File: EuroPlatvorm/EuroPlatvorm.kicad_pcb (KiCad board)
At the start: 2 copper layers, 32 parts, among them J1 Eurorack_Power_2x5, J2 USB_C_Receptacle_USB2.0, SW1 RST, SW2 BOOT, U1 TPS54202DDCR, U2 AMS1117-3.3, U3 USBLC6-2SC6, U4 ESP32-C6-WROOM-1-N4

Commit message: Fix tact switch footprint/symbol pin mismatch
- SW_TS-1187A footprint: renumber redundant legs to the switch's
  internal connection sets (left legs {1,3} -> pad 1, right legs
  {2,4} -> pad 2) so every pad carries a net
- PCB: applied same renumbering to placed SW1/SW2 instances and
  imported schematic net assignments via Update PCB from Schematic
- Resolves 'No net found for component SWx pad 3/4' warnings
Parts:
- added J3: Conn_01x14, Connector_PinHeader_2.54mm:PinHeader_1x14_P2.54mm_Vertical, F.Cu at (141.3, 69.8)
- added J4: Conn_01x14, Connector_PinHeader_2.54mm:PinHeader_1x14_P2.54mm_Vertical, F.Cu at (145.9, 69.8)
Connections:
- net Net-(U4-GPIO8) renamed /GPIO8
- net Net-(U4-GPIO9) renamed /GPIO9
- C10 pad 1: +3V3 -> GND
- C10 pad 2: GND -> +3V3
- C11 pad 1: +3V3 -> GND
- C11 pad 2: GND -> +3V3
- C6 pad 2: Net-(C6-Pad2) -> Net-(U1-FB)
- J1 pad 1: unconnected-(J1-Pin_1-Pad1) -> /-12V
- J1 pad 2: unconnected-(J1-Pin_2-Pad2) -> /-12V
- R1 pad 2: Net-(C6-Pad2) -> Net-(U1-FB)
- R2 pad 1: Net-(C6-Pad2) -> Net-(U1-FB)
- U1 pad 4: +3V3 -> Net-(U1-FB)
- U4 pad 11: unconnected-(U4-GPIO10-Pad11) -> /GPIO10
- U4 pad 12: unconnected-(U4-GPIO11-Pad12) -> /GPIO11
- U4 pad 16: unconnected-(U4-GPIO18-Pad16) -> /GPIO18
- U4 pad 17: unconnected-(U4-GPIO19-Pad17) -> /GPIO19
- U4 pad 18: unconnected-(U4-GPIO20-Pad18) -> /GPIO20
- U4 pad 19: unconnected-(U4-GPIO21-Pad19) -> /GPIO21
- U4 pad 20: unconnected-(U4-GPIO22-Pad20) -> /GPIO22
- U4 pad 21: unconnected-(U4-GPIO23-Pad21) -> /GPIO23
- U4 pad 23: unconnected-(U4-GPIO15-Pad23) -> /GPIO15
- U4 pad 24: unconnected-(U4-U0RXD/GPIO17-Pad24) -> /GPIO17
- U4 pad 25: unconnected-(U4-U0TXD/GPIO16-Pad25) -> /GPIO16
- U4 pad 26: unconnected-(U4-GPIO3/ADC1_CH3-Pad26) -> /GPIO3
- U4 pad 27: unconnected-(U4-GPIO2/ADC1_CH2-Pad27) -> /GPIO2
- U4 pad 4: unconnected-(U4-MTMS/GPIO4/ADC1_CH4-Pad4) -> /GPIO4
- U4 pad 5: unconnected-(U4-MTDI/GPIO5/ADC1_CH5-Pad5) -> /GPIO5
- U4 pad 6: unconnected-(U4-MTCK/GPIO6/ADC1_CH6-Pad6) -> /GPIO6
- U4 pad 7: unconnected-(U4-MTDO/GPIO7-Pad7) -> /GPIO7
- U4 pad 8: unconnected-(U4-GPIO0/ADC1_CH0/XTAL_32K_P-Pad8) -> /GPIO0
- U4 pad 9: unconnected-(U4-GPIO1/ADC1_CH1/XTAL_32K_N-Pad9) -> /GPIO1

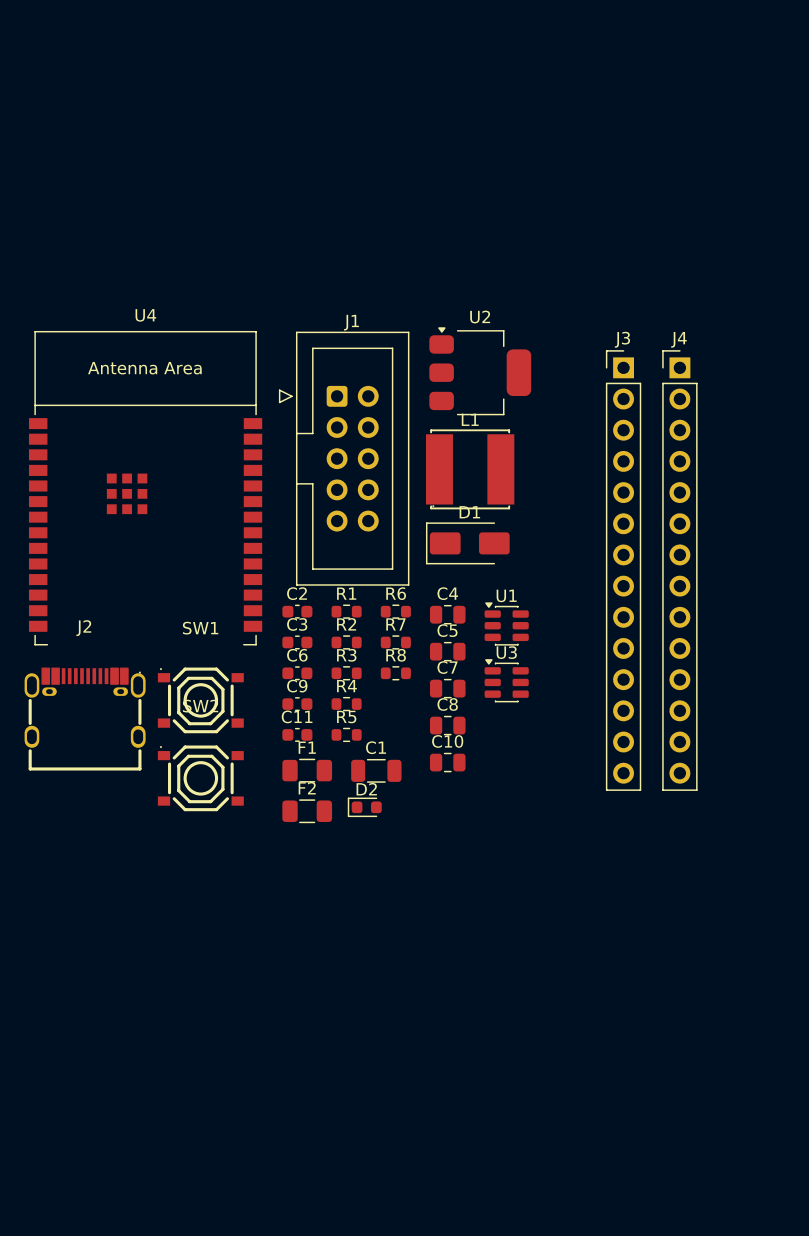
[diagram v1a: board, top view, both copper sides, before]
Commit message: Route EuroPlatvorm manually; fix GPIO labels and USB-C shell pad drills
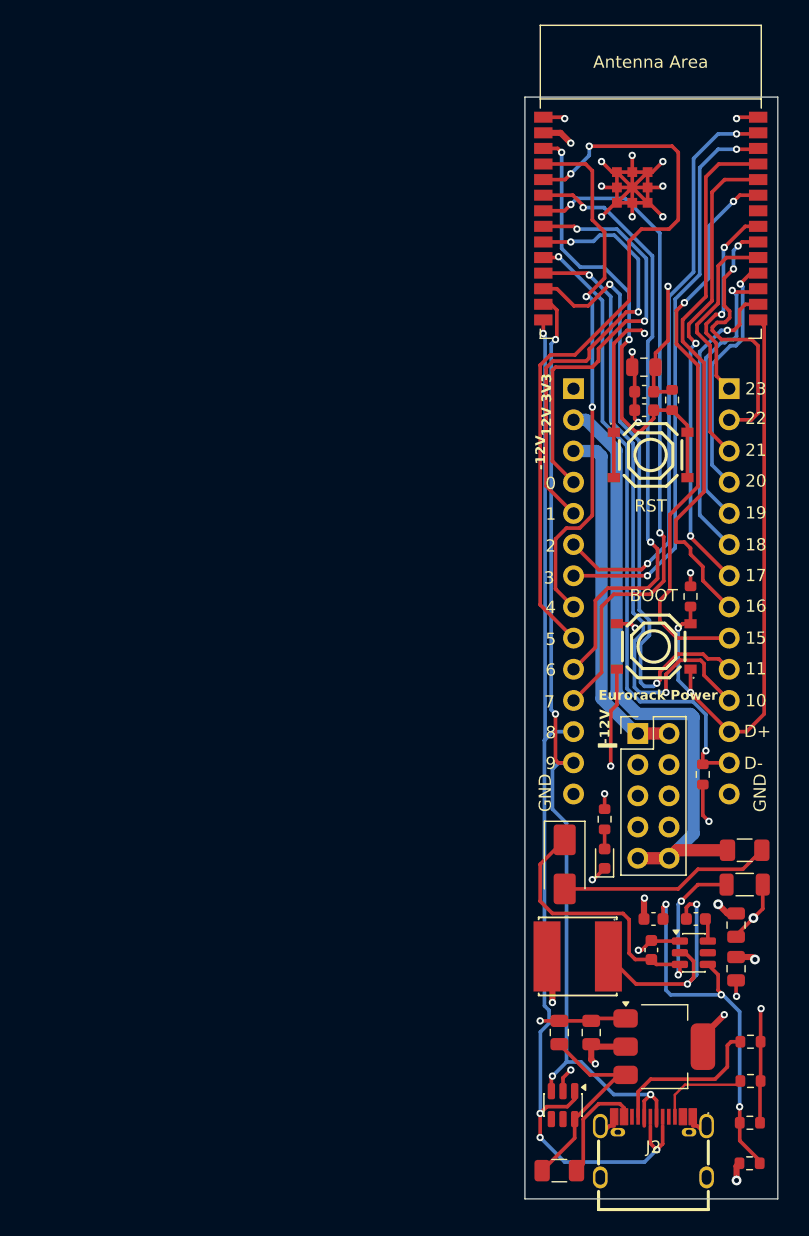
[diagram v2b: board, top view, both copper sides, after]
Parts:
- J1: footprint Connector_IDC:IDC-Header_2x05_P2.54mm_Vertical -> Connector_PinHeader_2.54mm:PinHeader_2x05_P2.54mm_Vertical
- J3, J4: moved to B.Cu
- moved J2 58.6 mm to (143.7, 133.3)
- moved U2 56.9 mm to (144.6, 125.1)
- moved R1 55.6 mm to (151.6, 134.6)
- moved R2 51.1 mm to (151.6, 131.3)
- moved U4 48.1 mm to (143.5, 57.6)
- moved R4 45.0 mm to (151.6, 127.9)
- moved R3 44.5 mm to (151.6, 124.7)
- moved SW1 41.7 mm to (143.5, 76.9)
- moved L1 40.6 mm to (137.6, 117.8), turned to 180 degrees
- moved C2 39.9 mm to (143.6, 117.2), turned to 90 degrees
- moved C11 39.7 mm to (143.0, 71.8)
- moved C3 39.5 mm to (147.2, 114.7)
- moved SW2 38.4 mm to (143.8, 92.5), turned to 180 degrees
- moved R5 38.0 mm to (145.2, 72.4), turned to -90 degrees
- moved C4 37.2 mm to (150.5, 118.8), turned to -90 degrees
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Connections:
- J3 pad 12: /GPIO10 -> /USB_DP
- J3 pad 13: /GPIO15 -> /USB_DM
- J4 pad 1: /GPIO18 -> /GPIO23
- J4 pad 10: /GPIO8 -> /GPIO11
- J4 pad 11: /GPIO11 -> /GPIO10
- J4 pad 12: /USB_DM -> /GPIO9
- J4 pad 13: /USB_DP -> /GPIO8
- J4 pad 2: /GPIO19 -> /GPIO22
- J4 pad 3: /GPIO20 -> /GPIO21
- J4 pad 4: /GPIO21 -> /GPIO20
- J4 pad 5: /GPIO22 -> /GPIO19
- J4 pad 6: /GPIO23 -> /GPIO18
- J4 pad 7: /GPIO16 -> /GPIO17
- J4 pad 8: /GPIO17 -> /GPIO16
- J4 pad 9: /GPIO9 -> /GPIO15
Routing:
- net GND: track 0.00 -> 99.9 mm, vias 0 -> 22
- net /USB_DP: track 0.00 -> 88.8 mm, vias 0 -> 4
- net /USB_DM: track 0.00 -> 82.5 mm, vias 0 -> 4
- net /GPIO5: track 0.00 -> 60.6 mm, vias 0 -> 2
- net /GPIO7: track 0.00 -> 54.1 mm, vias 0 -> 2
- net /GPIO8: track 0.00 -> 52.4 mm, vias 0 -> 2
- net +12V: track 0.00 -> 51.3 mm
- net /GPIO10: track 0.00 -> 51.3 mm, vias 0 -> 2
- net /GPIO9: track 0.00 -> 50.4 mm, vias 0 -> 2
- net /GPIO11: track 0.00 -> 50.1 mm, vias 0 -> 2
- net /GPIO6: track 0.00 -> 50.0 mm, vias 0 -> 2
- net /GPIO2: track 0.00 -> 47.8 mm, vias 0 -> 2
- net /GPIO15: track 0.00 -> 46.6 mm, vias 0 -> 2
- net /GPIO3: track 0.00 -> 46.4 mm, vias 0 -> 2
- net /GPIO16: track 0.00 -> 44.4 mm
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- added copper zone on In2.Cu, net +3V3
- added copper zone on In1.Cu, net GND
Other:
- board outline added: 20.6 x 89.8 mm
- copper layers 2 -> 4
- board text added: "-12V"
- board text added: "0"
- board text added: "1"
- board text added: "10"
- board text added: "11"
- board text added: "12V"
- board text added: "15"
- board text added: "16"
- board text added: "17"
- board text added: "18"
- board text added: "19"
- board text added: "2"
- board text added: "20"
- board text added: "21"
- board text added: "22"
- board text added: "23"
- board text added: "3"
- board text added: "3V3"
- board text added: "4"
- board text added: "5"
- board text added: "6"
- board text added: "7"
- board text added: "8"
- board text added: "9"
- board text added: "D+"
- board text added: "D-"
- board text added: "Eurorack Power"
- board text added: "GND"

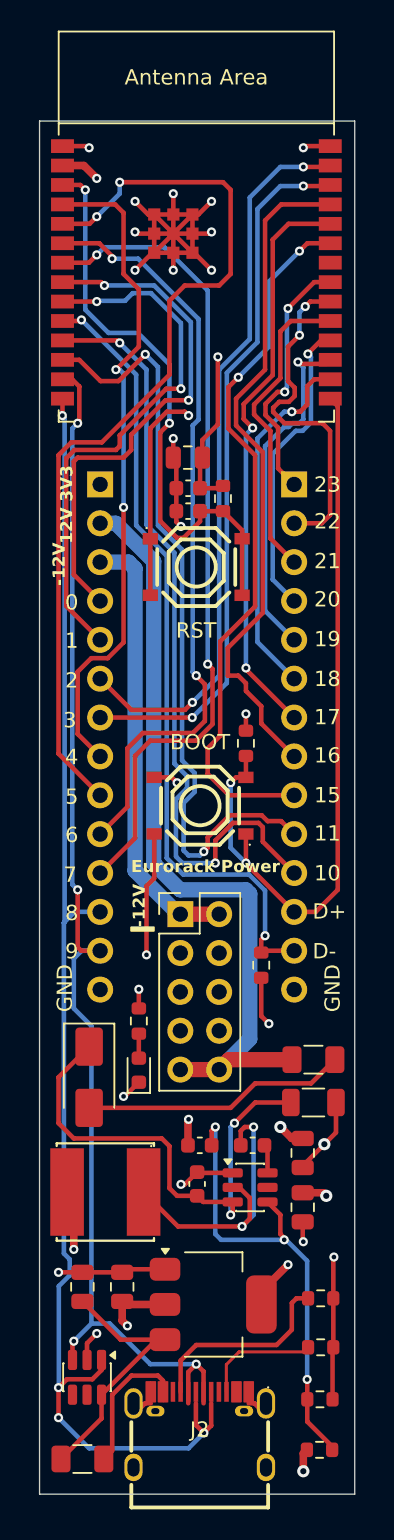
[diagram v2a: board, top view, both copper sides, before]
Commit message: Fix EMI review findings: C11 decoupling at 3V3 pin, buck SW/FB hot loop, USB routing, Vout to 3.3V
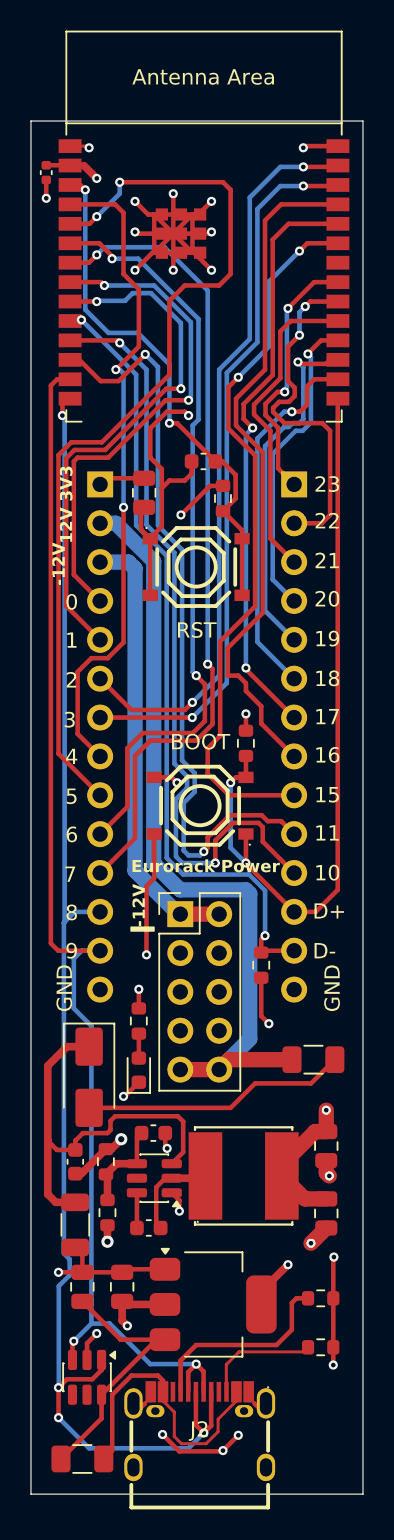
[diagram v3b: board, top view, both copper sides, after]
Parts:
- C11: footprint Capacitor_SMD:C_0603_1608Metric -> Capacitor_SMD:C_0402_1005Metric
- R2: value 21k -> 22k
- moved C11 22.6 mm to (133.7, 51.1), turned to 90 degrees
- moved R2 20.9 mm to (137.6, 115.8), turned to 90 degrees
- moved R1 20.8 mm to (137.7, 119.1), turned to 90 degrees
- moved C1 17.5 mm to (135.6, 119.9), turned to -90 degrees
- moved L1 9.10 mm to (146.6, 116.7), turned to 0 degrees
- moved C3 8.67 mm to (140.4, 120.1), turned to 180 degrees
- moved C2 8.09 mm to (135.6, 115.8), turned to -90 degrees
- moved U1 6.29 mm to (140.8, 116.8), turned to 180 degrees
- moved C10 3.66 mm to (140.1, 72.0), turned to 90 degrees
- moved C9 3.40 mm to (144.0, 70.0)
- moved C6 3.14 mm to (140.7, 113.9), turned to 180 degrees
- moved C5 1.60 mm to (152.0, 114.8)
- moved C4 1.59 mm to (152.0, 119.2)
- moved U4 0.50 mm to (144.0, 57.6)
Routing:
- net Net-(U1-FB): track 31.0 -> 6.16 mm, vias 3 -> 0
- net Net-(U1-SW): track 19.5 -> 6.30 mm, vias 2 -> 0
- net Net-(F2-Pad2): track 9.13 -> 18.8 mm
- net Net-(U4-EN/CHIP_PU): track 38.6 -> 33.6 mm
- net Net-(D1-K): track 32.2 -> 27.6 mm, vias 2 -> 0
- net +3V3: track 37.3 -> 34.2 mm, vias 12 -> 10
- net GND: track 99.9 -> 102.8 mm, vias 22 -> 26
- net /USB_DP: track 88.8 -> 90.3 mm
- net /GPIO8: track 52.4 -> 51.2 mm
- net /GPIO11: track 50.1 -> 49.0 mm
- net /GPIO9: track 50.4 -> 49.7 mm
- net /GPIO0: track 34.2 -> 33.6 mm
- net /USB_DM: track 82.5 -> 82.6 mm, vias 4 -> 2
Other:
- board size 20.6 x 89.8 mm -> 21.7 x 89.8 mm

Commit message: Harden USB-C footprint, add stitching and LDO thermal vias; relax edge clearance to 0.3mm
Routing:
- net GND: track 102.8 -> 95.7 mm, vias 26 -> 28
- net +3V3: vias 10 -> 14
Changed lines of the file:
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@@
 			)
 		)
-		(pad "" thru_hole oval
+		(pad "" np_thru_hole oval
 			(at -2.9 -1.21)
-			(size 1.2 0.8)
+			(size 0.55 0.5)
 			(drill oval 0.55 0.5)
 			(layers "*.Cu" "*.Mask")
-			(remove_unused_layers no)
 		)
-		(pad "" thru_hole oval
+		(pad "" np_thru_hole oval
 			(at 2.9 -1.21)
-			(size 1.2 0.8)
+			(size 0.55 0.5)
 			(drill oval 0.55 0.5)
 			(layers "*.Cu" "*.Mask")
-			(remove_unused_layers no)
 		)
 		(pad "1" thru_hole oval
@@
 				(gr_poly
 					(pts
-						(xy 0.299923 0.649935) (xy 0.299923 -0.650088) (xy -0.000076 -0.650088) (xy -0.000076 -0.649935)
-						(xy -0.30005 -0.649935) (xy -0.30005 0.650088) (xy -0.000051 0.650088) (xy -0.000051 0.649935)
-						(xy 0.299923 0.649935)
+						(xy 0.15 0.649935) (xy 0.15 -0.650088) (xy -0.000076 -0.650088) (xy -0.000076 -0.649935) (xy -0.30005 -0.649935)
+						(xy -0.30005 0.650088) (xy -0.000051 0.650088) (xy -0.000051 0.649935) (xy 0.15 0.649935)
 					)
 					(width 0.1)
@@
 				(gr_poly
 					(pts
-						(xy 0.300076 0.650037) (xy 0.300076 -0.649935) (xy 0.000051 -0.649935) (xy 0.000051 -0.64991)
-						(xy -0.299898 -0.64991) (xy -0.299898 0.650062) (xy 0.000127 0.650062) (xy 0.000127 0.650037)
-						(xy 0.300076 0.650037)
+						(xy 0.24 0.650037) (xy 0.24 -0.649935) (xy 0.000051 -0.649935) (xy 0.000051 -0.64991) (xy -0.2 -0.64991)
+						(xy -0.2 0.650062) (xy 0.000127 0.650062) (xy 0.000127 0.650037) (xy 0.24 0.650037)
 					)
 					(width 0.1)
@@
 				(gr_poly
 					(pts
-						(xy -0.300152 -0.650088) (xy -0.300152 0.649884) (xy -0.000152 0.649884) (xy -0.000127 0.649884)
-						(xy 0.299872 0.649884) (xy 0.299872 -0.650088) (xy -0.000127 -0.650088) (xy -0.000152 -0.650088)
-						(xy -0.300152 -0.650088)
+						(xy -0.15 -0.650088) (xy -0.15 0.649884) (xy -0.000152 0.649884) (xy -0.000127 0.649884) (xy 0.299872 0.649884)
+						(xy 0.299872 -0.650088) (xy -0.000127 -0.650088) (xy -0.000152 -0.650088) (xy -0.15 -0.650088)
 					)
 					(width 0.1)
@@
 				(gr_poly
 					(pts
-						(xy 0.299872 0.649884) (xy 0.299872 -0.650088) (xy -0.000127 -0.650088) (xy -0.000152 -0.650088)
-						(xy -0.300152 -0.650088) (xy -0.300152 0.649884) (xy -0.000152 0.649884) (xy -0.000127 0.649884)
-						(xy 0.299872 0.649884)
+						(xy 0.2 0.649884) (xy 0.2 -0.650088) (xy -0.000127 -0.650088) (xy -0.000152 -0.650088) (xy -0.24 -0.650088)
+						(xy -0.24 0.649884) (xy -0.000152 0.649884) (xy -0.000127 0.649884) (xy 0.2 0.649884)
 					)
 					(width 0.1)
@@
 	)
 	(segment
-		(start 146.25 133.65)
-		(end 145.25 134.65)
-		(width 0.3)
-		(layer "F.Cu")
-		(net "GND")
-	)
-	(segment
 		(start 141.9 90.65)
 		(end 142.25 91)
@@
 	)
 	(segment
+		(start 147.69 131.57)
+		(end 146.93 130.81)
+		(width 0.2)
+		(layer "F.Cu")
+		(net "GND")
+	)
+	(segment
 		(start 139.61 55.11)
 		(end 139.5 55)
@@
 	)
 	(segment
-		(start 142.005 55.11)
-		(end 140.755 53.86)
+		(start 135.6 116.55)
+		(end 135.6 117.2)
 		(width 0.3)
 		(layer "F.Cu")
@@
 	)
 	(segment
-		(start 141.3 133.6)
-		(end 142.4 134.7)
+		(start 142.005 55.11)
+		(end 140.755 53.86)
 		(width 0.3)
 		(layer "F.Cu")
@@
 	)
 	(segment
-		(start 136 116.55)
-		(end 137.6 114.95)
-		(width 0.5)
-		(layer "F.Cu")
-		(net "GND")
-	)
-	(segment
 		(start 143.255 53.86)
 		(end 143.64 53.86)
@@
 	)
 	(segment
+		(start 139.4 131.57)
+		(end 139.77 131.57)
+		(width 0.2)
+		(layer "F.Cu")
+		(net "GND")
+	)
+	(segment
 		(start 138.75 111.5)
 		(end 138.825 111.5)
@@
 	)
 	(segment
-		(start 142.4 134.7)
-		(end 145.2 134.7)
-		(width 0.3)
-		(layer "F.Cu")
-		(net "GND")
-	)
-	(segment
 		(start 138.66 123)
 		(end 136.06 123)
@@
 	)
 	(segment
+		(start 148.06 131.57)
+		(end 147.69 131.57)
+		(width 0.2)
+		(layer "F.Cu")
+		(net "GND")
+	)
+	(segment
 		(start 141.25 71.75)
 		(end 141.25 70.5)
@@
 	)
 	(segment
-		(start 140.16 131.56)
-		(end 139.4 132.32)
-		(width 0.3)
-		(layer "F.Cu")
-		(net "GND")
-	)
-	(segment
 		(start 152.26 49.39)
 		(end 150.61 49.39)
@@
 	)
 	(segment
-		(start 142.005 53.86)
-		(end 142.005 52.505)
-		(width 0.3)
+		(start 139.77 131.57)
+		(end 140.53 130.81)
+		(width 0.2)
 		(layer "F.Cu")
 		(net "GND")
 	)
 	(segment
-		(start 140.755 56.36)
-		(end 142.005 55.11)
+		(start 142.005 53.86)
+		(end 142.005 52.505)
 		(width 0.3)
 		(layer "F.Cu")
@@
 	)
 	(segment
-		(start 145.25 134.65)
-		(end 145.2 134.7)
+		(start 140.755 56.36)
+		(end 142.005 55.11)
 		(width 0.3)
 		(layer "F.Cu")
@@
 	)
 	(segment
-		(start 135.6 116.55)
-		(end 136 116.55)
-		(width 0.5)
-		(layer "F.Cu")
-		(net "GND")
-	)
-	(segment
 		(start 140.75 94.35)
 		(end 140.75 97.25)
@@
 	)
 	(segment
-		(start 147.3 131.56)
-		(end 148.06 132.32)
-		(width 0.3)
-		(layer "F.Cu")
-		(net "GND")
-	)
-	(segment
 		(start 140.25 97.75)
 		(end 140.25 102.25)
@@
 	)
 	(via
+		(at 133.3 132.5)
+		(size 0.6)
+		(drill 0.3)
+		(layers "F.Cu" "B.Cu")
+		(free yes)
+		(net "GND")
+	)
+	(via
 		(at 143 67)
 		(size 0.6)
@@
 	)
 	(via
-		(at 145.25 134.65)
+		(at 152.5 122)
 		(size 0.6)
 		(drill 0.3)
 		(layers "F.Cu" "B.Cu")
+		(free yes)
 		(net "GND")
 	)
 	(via
-		(at 152.5 122)
+		(at 144.5 53)
 		(size 0.6)
 		(drill 0.3)
@@
 	)
 	(via
-		(at 144.5 53)
+		(at 139.5 55)
 		(size 0.6)
 		(drill 0.3)
@@
 	)
 	(via
-		(at 139.5 55)
+		(at 133.35 67)
 		(size 0.6)
 		(drill 0.3)
@@
 	)
 	(via
-		(at 138.75 111.5)
+		(at 144 135)
 		(size 0.6)
 		(drill 0.3)
@@
 	)
 	(via
-		(at 150.5 49.5)
+		(at 138.75 111.5)
 		(size 0.6)
 		(drill 0.3)
@@
 	)
 	(via
-		(at 146.25 133.65)
+		(at 135.6 117.2)
 		(size 0.6)
 		(drill 0.3)
@@
 	)
 	(via
+		(at 150.5 49.5)
+		(size 0.6)
+		(drill 0.3)
+		(layers "F.Cu" "B.Cu")
+		(free yes)
+		(net "GND")
+	)
+	(via
 		(at 133.7 52.8)
 		(size 0.6)
@@
 	)
 	(via
-		(at 142.4 119)
+		(at 133.4 130.6)
 		(size 0.6)
 		(drill 0.3)
 		(layers "F.Cu" "B.Cu")
+		(free yes)
 		(net "GND")
 	)
 	(via
-		(at 136.5 49.5)
+		(at 142.4 119)
 		(size 0.6)
 		(drill 0.3)
 		(layers "F.Cu" "B.Cu")
-		(free yes)
 		(net "GND")
 	)
 	(via
-		(at 142.25 91)
+		(at 136.5 49.5)
 		(size 0.6)
 		(drill 0.3)
 		(layers "F.Cu" "B.Cu")
+		(free yes)
 		(net "GND")
 	)
 	(via
-		(at 141.3 133.6)
+		(at 142.25 91)
 		(size 0.6)
 		(drill 0.3)
@@
 	)
 	(via
+		(at 147.16 126.05)
+		(size 0.6)
+		(drill 0.3)
+		(layers "F.Cu" "B.Cu")
+		(net "+3V3")
+	)
+	(via
 		(at 137 51.5)
 		(size 0.6)
@@
 	)
 	(via
+		(at 148.36 124.15)
+		(size 0.6)
+		(drill 0.3)
+		(layers "F.Cu" "B.Cu")
+		(net "+3V3")
+	)
+	(via
 		(at 142.5 73.5)
 		(size 0.6)
@@
 	)
 	(via
+		(at 147.16 124.15)
+		(size 0.6)
+		(drill 0.3)
+		(layers "F.Cu" "B.Cu")
+		(net "+3V3")
+	)
+	(via
 		(at 137.7 121)
 		(size 0.8)
@@
 		(layers "F.Cu" "B.Cu")
 		(net "+3V3")
+	)
+	(via
+		(at 148.36 126.05)
+		(size 0.6)
+		(drill 0.3)
+		(layers "F.Cu" "B.Cu")
+		(net "+3V3")
